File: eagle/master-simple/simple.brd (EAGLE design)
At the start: 73.3 x 43.4 mm, 43 parts, among them CON3 SPI, IC1 MCP1703CB, J1 RJ12RIGHTANGLE-I2C, J2 RJ12RIGHTANGLE-I2C, J3 RJ12RIGHTANGLE-I2C, X1 MINI-USB, X3 8MHz

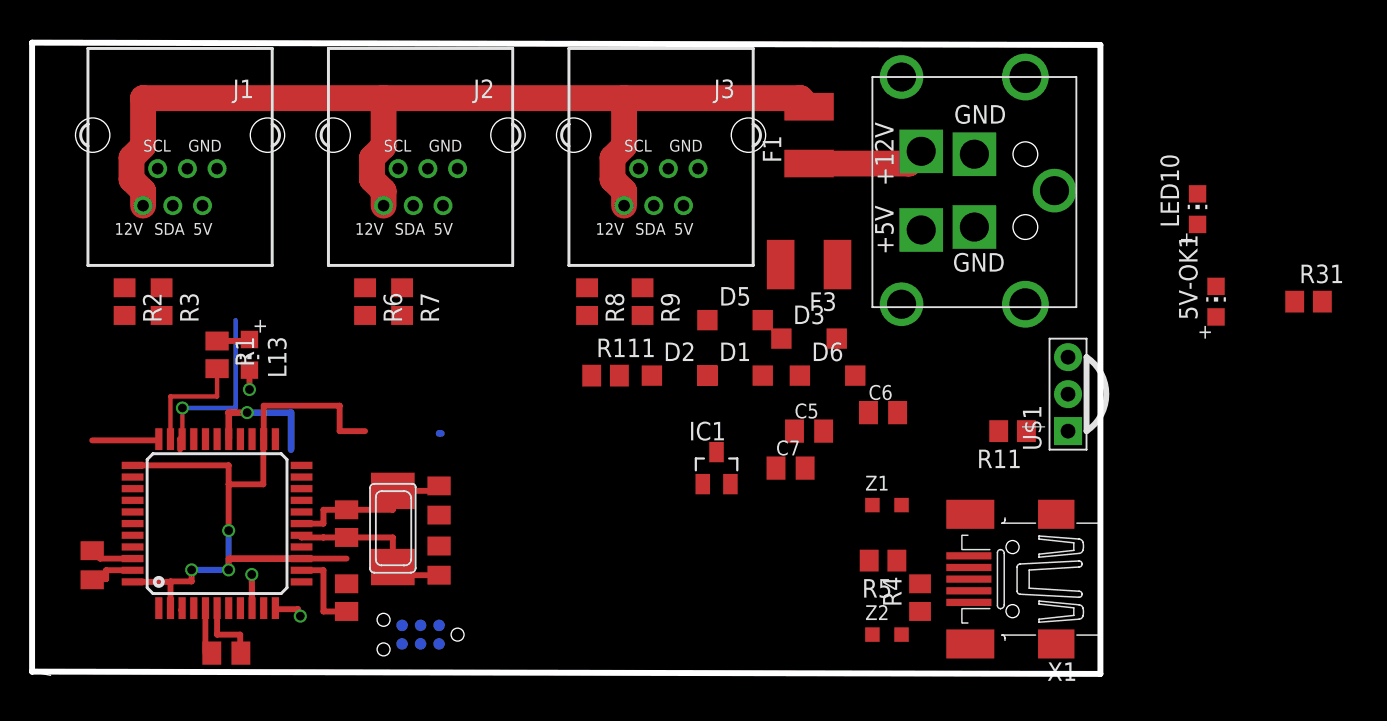
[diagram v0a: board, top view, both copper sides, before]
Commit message: finalize first version of master-simple
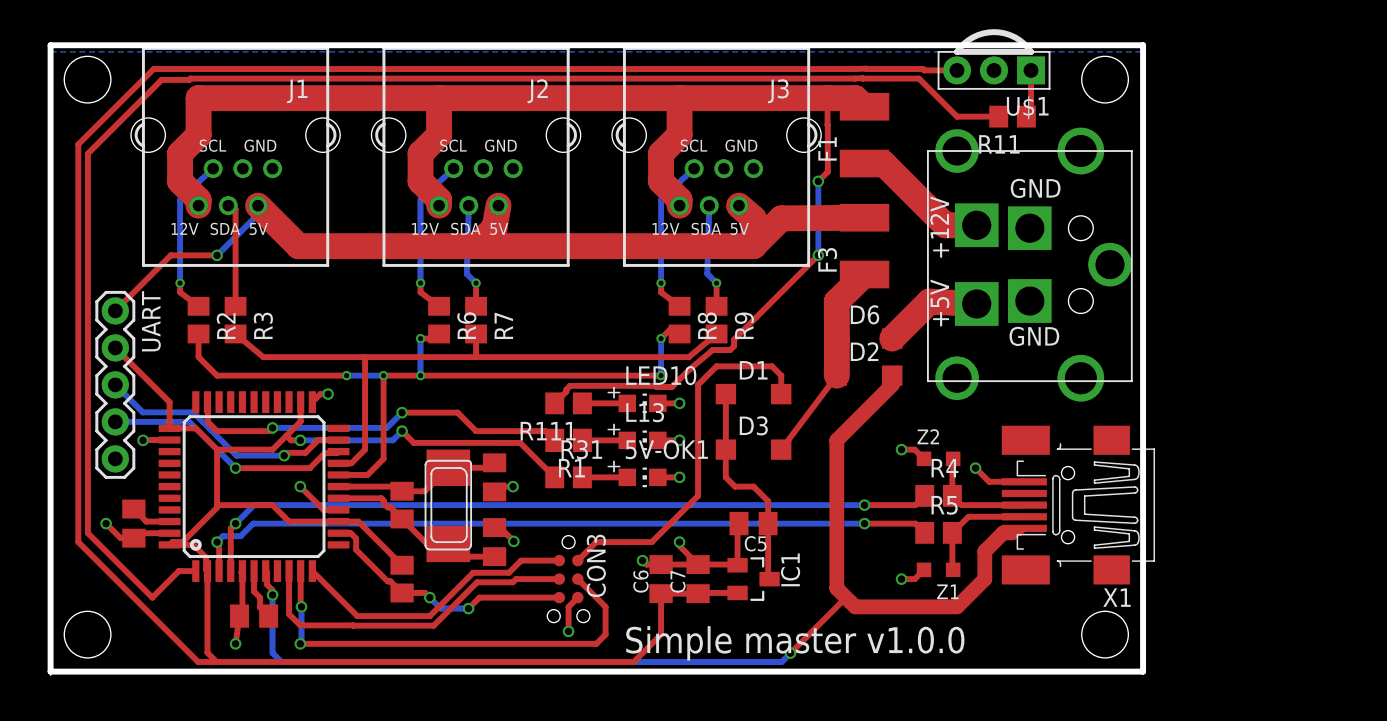
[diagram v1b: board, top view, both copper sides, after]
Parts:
- removed D5: Schottky, diode:SOD123
- added UART: (no value), SparkFun-Connectors:1X05
- L13: value RED -> BLUE
- R1: value 1k -> 10k
- moved R31 52.2 mm to (35.6, 13.3)
- moved 5V-OK1 41.2 mm to (40.6, 13.3), turned to 270 degrees
- moved LED10 40.4 mm to (40.6, 18.4), turned to 270 degrees
- moved L13 27.6 mm to (40.6, 15.9), turned to 270 degrees
- moved R1 24.8 mm to (35.6, 15.9), turned to 180 degrees
- moved U$1 22.8 mm to (64.8, 41.3), turned to 180 degrees
- moved R11 21.6 mm to (66.0, 38.1)
- moved C6 19.1 mm to (41.9, 6.35), turned to 90 degrees
- moved D2 12.7 mm to (55.9, 20.3)
- moved Z2 12.6 mm to (61.0, 14.6)
- moved CON3 9.92 mm to (35.6, 8.89), flipped to the top, turned to 270 degrees
- moved C7 9.92 mm to (44.5, 6.35), turned to 90 degrees
- moved D3 8.52 mm to (48.3, 15.2)
- moved IC1 8.03 mm to (48.3, 6.35), turned to 270 degrees
- moved C5 7.41 mm to (48.3, 10.2), turned to 180 degrees
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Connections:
- removed net +3.3: C6.1, C7.1, IC1.2, R15.2, R31.1, U$1.3, U$4.14, U$4.2, U$4.24, U$4.34, U$4.44
- removed net VCC-FTDI: D5.A
- new net +3V3: C6.1, C7.1, IC1.2, R15.2, R31.1, U$1.3, U$4.14, U$4.2, U$4.24, U$4.34, U$4.44, UART.2
- net +5V: now also UART.1
- net +XV: no longer D5.C
- net GND: now also UART.5
- net RX: now also UART.4
- net TX: now also UART.3
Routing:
- net +3V3: track 0.00 -> 214.2 mm, vias 0 -> 2
- net D7: track 0.00 -> 101.8 mm
- net VUSB: track 0.00 -> 80.4 mm, vias 0 -> 2
- net +5V: track 0.00 -> 63.3 mm, vias 0 -> 1
- net +3.3: track 53.5 -> 0.00 mm, vias 3 -> 0
- net RD+: track 0.02 -> 51.5 mm, vias 0 -> 2
- net RD-: track 0.20 -> 51.4 mm, vias 0 -> 2
- net SCL: track 0.00 -> 51.2 mm, vias 0 -> 6
- net SDA: track 0.00 -> 44.3 mm
- net GND: track 7.85 -> 45.7 mm, vias 1 -> 16
- net +12V: track 70.1 -> 105.0 mm, vias 0 -> 2
- net MOSI: track 0.00 -> 30.9 mm, vias 0 -> 2
- net VCC-ICSP: track 0.00 -> 25.5 mm
- net SCK: track 3.90 -> 23.2 mm, vias 1 -> 0
- net D13: track 8.04 -> 26.9 mm, vias 0 -> 2
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- added copper zone on layer 16, net GND
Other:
- board size 73.3 x 43.4 mm -> 75 x 43.3 mm
- board text added: "Simple master v1.0.0"
- board text removed: "D6"
